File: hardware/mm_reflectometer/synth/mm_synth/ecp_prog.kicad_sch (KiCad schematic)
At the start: 92 parts

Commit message: adding digital connections to synth schematic
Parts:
- removed C? (x3): 100 nF, Capacitor_SMD:C_0402_1005Metric, symbol Device:C
- added C? (x3): 100 nF, symbol Device:C_Small
- added U?: ECP5U_25_CABGA256, Package_BGA:BGA-256_14.0x14.0mm_Layout16x16_P0.8mm_Ball0.45mm_Pad0.32mm_NSMD, symbol Lattice_ECP5:ECP5U_25_CABGA256
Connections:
- net +3V3: now also C?.1, C?.1, C?.1
- net GND: now also C?.2, C?.2, C?.2, U?.A1 (GND[27]), U?.A16 (GND[27]), U?.D15 (GND[27]), U?.D2 (GND[27]), U?.F8 (GND[27]), U?.F9 (GND[27]), U?.G10 (GND[27]), U?.G8 (GND[27]), U?.H1 (GND[27]), U?.H10 (GND[27]), U?.H16 (GND[27]), U?.H8 (GND[27]), U?.H9 (GND[27]), U?.J10 (GND[27]), U?.J8 (GND[27]), U?.J9 (GND[27]), U?.K10 (GND[27]), U?.K6 (GND[27]), U?.K7 (GND[27]), U?.K8 (GND[27]), U?.K9 (GND[27]), U?.N15 (GND[27]), U?.N2 (GND[27]), U?.T1 (GND[27]), U?.T12 (GND[27]), U?.T16 (GND[27]), U?.T5 (GND[27])
- new net +1V1: U?.G6 (VCC[6]), U?.G7 (VCC[6]), U?.G9 (VCC[6]), U?.L10 (VCC[6]), U?.L8 (VCC[6]), U?.L9 (VCC[6])
- new net +2V5: U?.G11 (VCCAUX[2]), U?.L7 (VCCAUX[2])
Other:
- note added: "TODO: ADD RESET BUTTON.."
- note removed: "TODO: ADD RESET.."
- moved on the sheet: R?, TP?, U?H

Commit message: work on mm synth schematic - control signals and footprint assignments
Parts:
- added C1621, C1622: 100 nF, Capacitor_SMD:C_0402_1005Metric, symbol Device:C_Small
- added J1605, J1606: Conn_Coaxial, Connector_Coaxial:U.FL_Hirose_U.FL-R-SMT-1_Vertical, symbol Connector:Conn_Coaxial
- added R1638, R1639: 5.1k, Resistor_SMD:R_0402_1005Metric, symbol Device:R_Small
- added SW1601, SW1602: SW_Push, symbol Switch:SW_Push
- added TP1604: TestPoint, TestPoint:TestPoint_Pad_D1.5mm, symbol Connector:TestPoint
- C1623, C1624, C1625: renamed from C?; footprint (none) -> Capacitor_SMD:C_0402_1005Metric
- U1605: renamed from U?; Notes (none) -> Flash schematic and symbol adapted from Greg Davill's ECPBr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
- gave numbers to parts that had none: 82
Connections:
- net +3V3: now also R1638.1, R1639.1
- net GND: now also C1621.2, C1622.2, J1605.2 (Ext), J1606.2 (Ext), SW1601.1, SW1602.1
- net at U1601.L13 (PR29C/+/GR_PCLK3_1/RDQ32): now also TP1604.1
- net at U1601.B7 (PT27B/-/PCLKC0_1): now also C1622.1, R1639.2, SW1602.2
- net at U1601.C5 (PT15A/+): now also C1621.1, R1638.2, SW1601.2
- net at U1601.D7 (PT24B/-/GR_PCLK0_0): now also J1606.1 (In)
- net at U1601.E7 (PT24A/+/GR_PCLK0_1): now also J1605.1 (In)
- net FLASH_~HLD~|~RST~|IO3 renamed FLASH_~{HLD}|~{RST}|IO3
- net FLASH_~WP~|IO2 renamed FLASH_~{WP}|IO2
- net ~FPGA_RESET renamed ~{FPGA_RESET}
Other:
- note removed: "Flash and sequencer schematic and symbol adapted from Greg Davill's ECPBreaker CC-BY-SA V4.0"
- note removed: "TODO: ADD RESET BUTTON.."
- moved on the sheet: C1625, U1601B

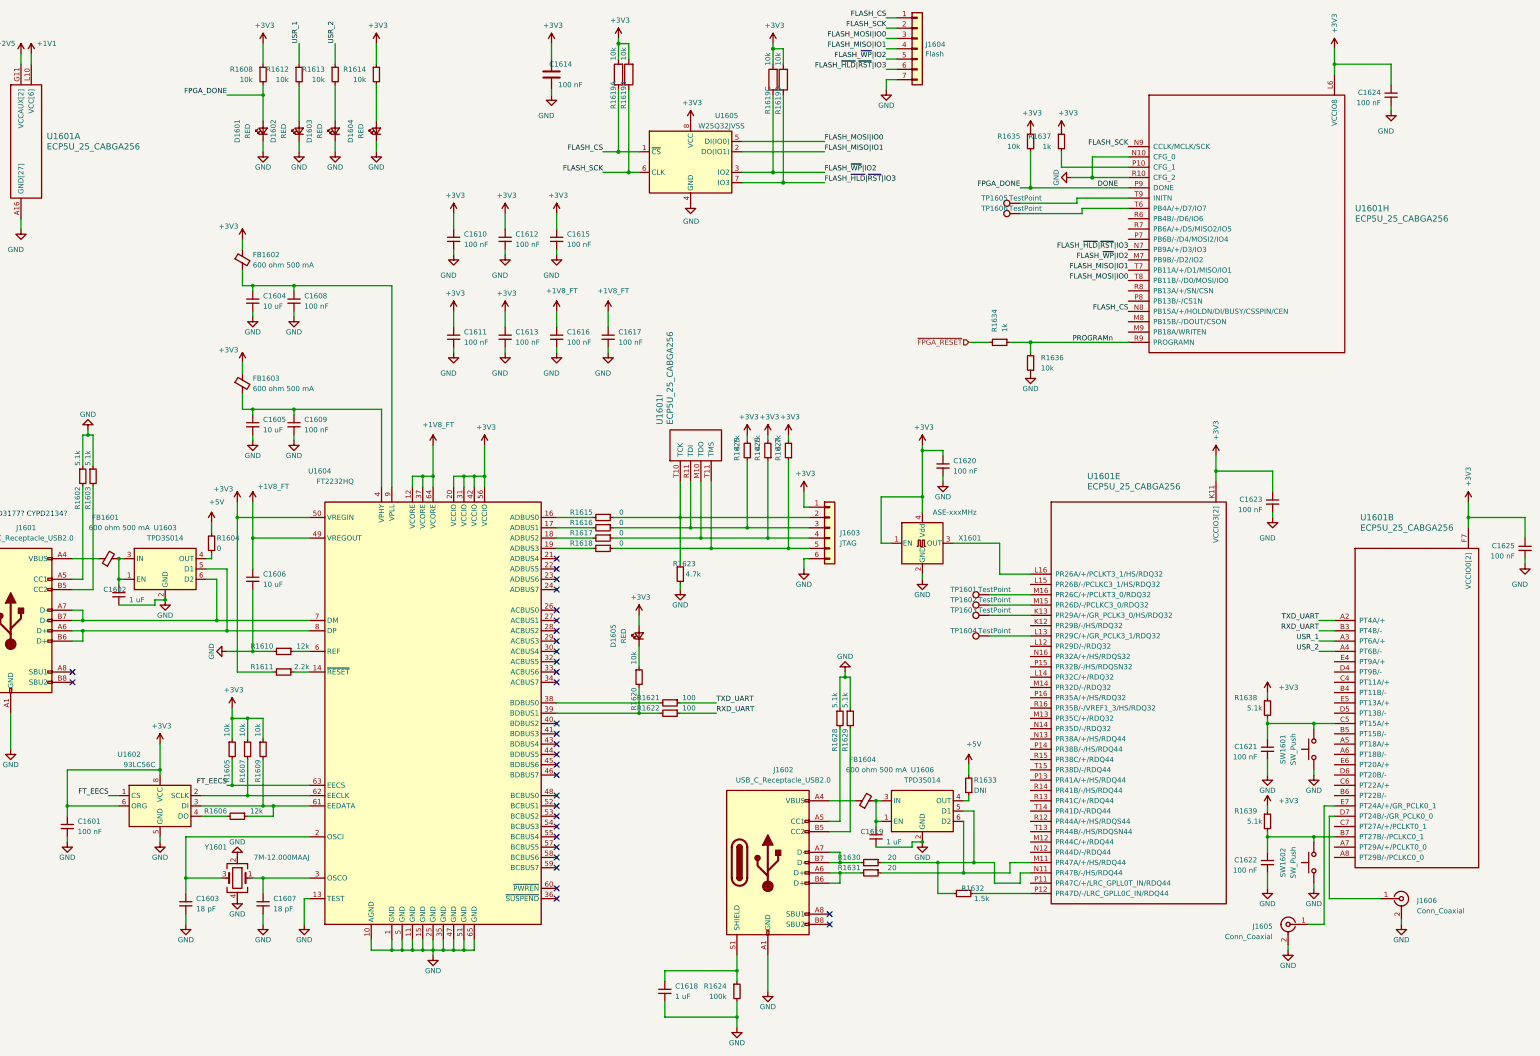
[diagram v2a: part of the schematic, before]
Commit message: added aux high speed io connector, fixed hierarchical buses
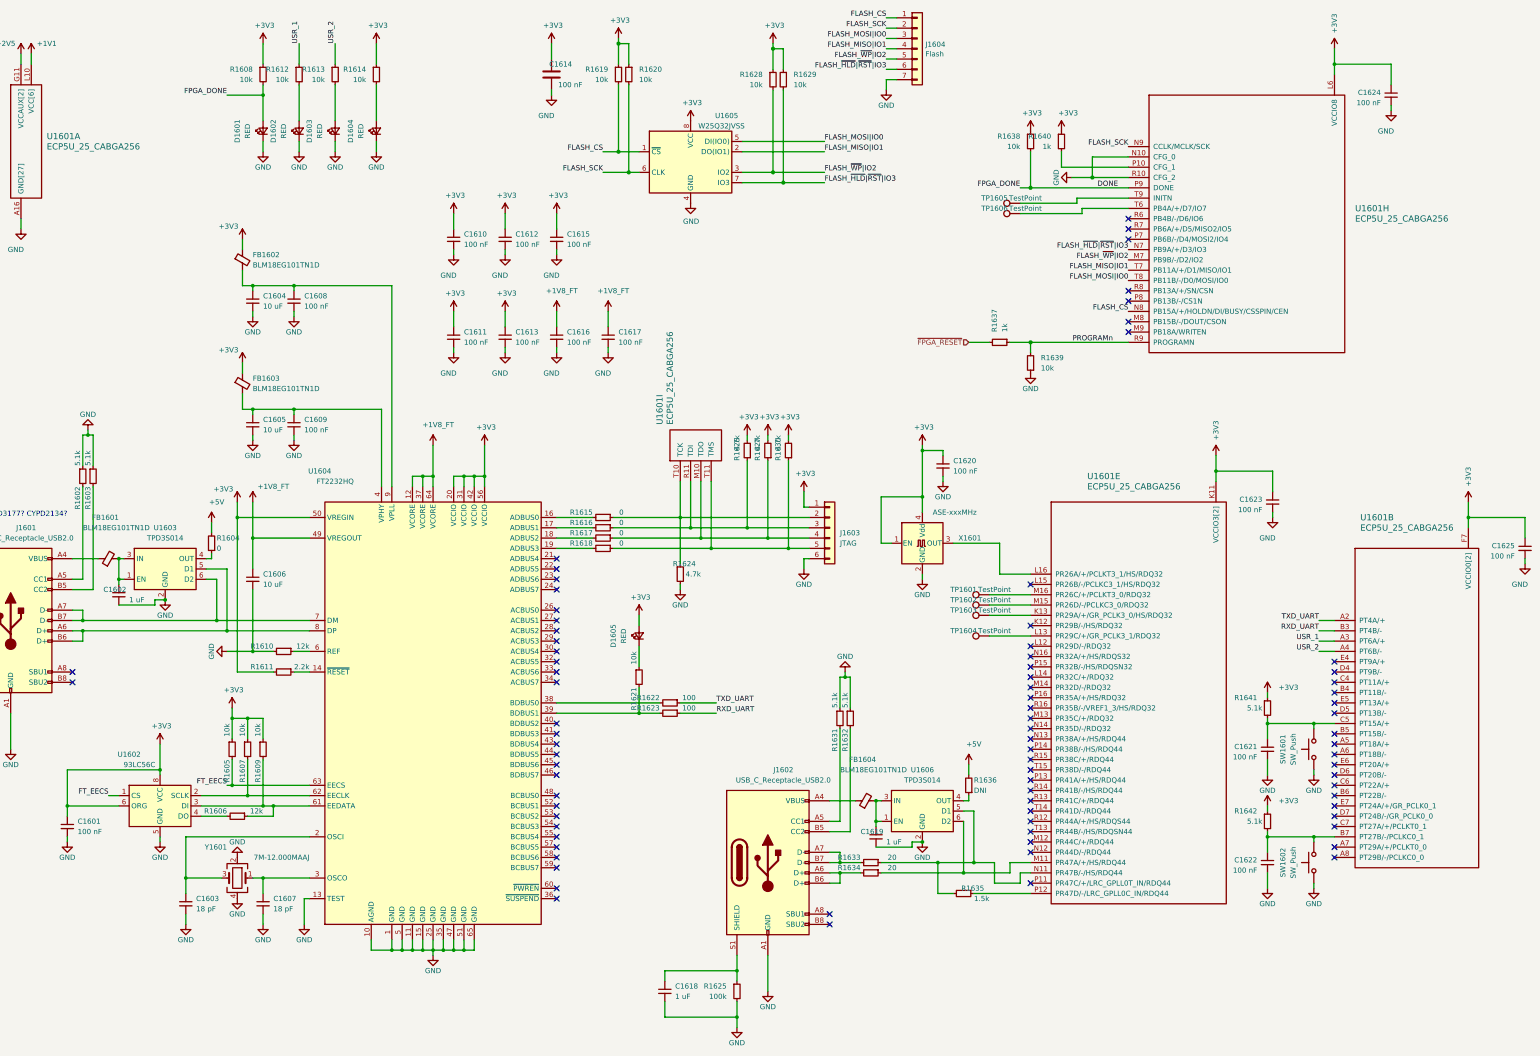
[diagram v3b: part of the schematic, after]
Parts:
- removed J1605, J1606: Conn_Coaxial, Connector_Coaxial:U.FL_Hirose_U.FL-R-SMT-1_Vertical, symbol Connector:Conn_Coaxial
- removed R1619: 10k, Resistor_SMD:R_Array_Convex_4x0402, symbol Device:R_Pack04_Split
- added R1619, R1620, R1628, R1629: 10k, Resistor_SMD:R_0402_1005Metric, symbol Device:R_Small
- FB1601, FB1602, FB1603, FB1604: value 600 ohm 500 mA -> BLM18EG101TN1D
- SW1601, SW1602: footprint (none) -> Button_Switch_SMD:SW_SPST_CK_KXT3
- renumbered R1620 to R1621, R1621 to R1622, R1622 to R1623, R1623 to R1624, R1624 to R1625, R1625 to R1626, R1626 to R1627, R1627 to R1630, R1628 to R1631, R1629 to R1632, R1630 to R1633, R1631 to R1634, R1632 to R1635, R1633 to R1636, R1634 to R1637, R1635 to R1638, R1636 to R1639, R1637 to R1640, R1638 to R1641, R1639 to R1642
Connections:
- net +3V3: now also R1619.1, R1620.1, R1628.1, R1629.1
- net FLASH_CS: now also R1619.2
- net FLASH_SCK: now also R1620.2
- net FLASH_~{HLD}|~{RST}|IO3: now also R1629.2
- net FLASH_~{WP}|IO2: now also R1628.2
- no-connect marks 32 -> 81

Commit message: schematic cleanup, erc
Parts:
- U1601: symbol Lattice_ECP5:ECP5U_25_CABGA256 -> jtk_rf:ECP5U_25_CABGA256
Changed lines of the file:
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@@
     (pin "7")
   )
-  (symbol (lib_id "Lattice_ECP5:ECP5U_25_CABGA256") (at 196.85 135.89 90) (unit 9)
+  (symbol (lib_id "jtk_rf:ECP5U_25_CABGA256") (at 196.85 135.89 90) (unit 9)
     (in_bom yes) (on_board yes)
     (property "Reference" "U1601" (id 0) (at 191.77 121.92 0)
@@
       (effects (font (size 1.524 1.524)) (justify left))
     )
-    (property "Footprint" "Package_BGA:BGA-256_14.0x14.0mm_Layout16x16_P0.8mm_Ball0.45mm_Pad0.32mm_NSMD" (id 2) (at 195.58 132.08 0)
-      (effects (font (size 1.524 1.524)) (justify right) hide)
-    )
-    (property "Datasheet" "" (id 3) (at 200.66 132.08 0)
-      (effects (font (size 1.524 1.524)) (justify right) hide)
-    )
-    (property "manf#" "ECP5U_25" (id 4) (at 198.12 132.08 0)
+    (property "Footprint" "Package_BGA:BGA-256_14.0x14.0mm_Layout16x16_P0.8mm_Ball0.45mm_Pad0.32mm_NSMD" (id 2) (at 195.58 139.7 0)
+      (effects (font (size 1.524 1.524)) (justify right) hide)
+    )
+    (property "Datasheet" "" (id 3) (at 200.66 139.7 0)
+      (effects (font (size 1.524 1.524)) (justify right) hide)
+    )
+    (property "manf#" "ECP5U_25" (id 4) (at 198.12 139.7 0)
       (effects (font (size 1.524 1.524)) (justify right) hide)
     )
@@
     (pin "6")
   )
-  (symbol (lib_id "Lattice_ECP5:ECP5U_25_CABGA256") (at 26.67 55.88 0) (unit 1)
+  (symbol (lib_id "jtk_rf:ECP5U_25_CABGA256") (at 26.67 55.88 0) (unit 1)
     (in_bom yes) (on_board yes)
     (property "Reference" "U1601" (id 0) (at 40.64 50.8 0)
@@
       (effects (font (size 1.524 1.524)) (justify left))
     )
-    (property "Footprint" "Package_BGA:BGA-256_14.0x14.0mm_Layout16x16_P0.8mm_Ball0.45mm_Pad0.32mm_NSMD" (id 2) (at 30.48 54.61 0)
-      (effects (font (size 1.524 1.524)) (justify right) hide)
-    )
-    (property "Datasheet" "" (id 3) (at 30.48 59.69 0)
-      (effects (font (size 1.524 1.524)) (justify right) hide)
-    )
-    (property "manf#" "ECP5U_25" (id 4) (at 30.48 57.15 0)
+    (property "Footprint" "Package_BGA:BGA-256_14.0x14.0mm_Layout16x16_P0.8mm_Ball0.45mm_Pad0.32mm_NSMD" (id 2) (at 22.86 54.61 0)
+      (effects (font (size 1.524 1.524)) (justify right) hide)
+    )
+    (property "Datasheet" "" (id 3) (at 22.86 59.69 0)
+      (effects (font (size 1.524 1.524)) (justify right) hide)
+    )
+    (property "manf#" "ECP5U_25" (id 4) (at 22.86 57.15 0)
       (effects (font (size 1.524 1.524)) (justify right) hide)
     )
@@
     (pin "S1")
   )
-  (symbol (lib_id "Lattice_ECP5:ECP5U_25_CABGA256") (at 358.14 170.18 0) (unit 2)
+  (symbol (lib_id "jtk_rf:ECP5U_25_CABGA256") (at 358.14 170.18 0) (unit 2)
     (in_bom yes) (on_board yes)
     (property "Reference" "U1601" (id 0) (at 364.49 144.78 0)
@@
       (effects (font (size 1.524 1.524)) (justify left))
     )
-    (property "Footprint" "Package_BGA:BGA-256_14.0x14.0mm_Layout16x16_P0.8mm_Ball0.45mm_Pad0.32mm_NSMD" (id 2) (at 361.95 168.91 0)
-      (effects (font (size 1.524 1.524)) (justify right) hide)
-    )
-    (property "Datasheet" "" (id 3) (at 361.95 173.99 0)
-      (effects (font (size 1.524 1.524)) (justify right) hide)
-    )
-    (property "manf#" "ECP5U_25" (id 4) (at 361.95 171.45 0)
+    (property "Footprint" "Package_BGA:BGA-256_14.0x14.0mm_Layout16x16_P0.8mm_Ball0.45mm_Pad0.32mm_NSMD" (id 2) (at 354.33 168.91 0)
+      (effects (font (size 1.524 1.524)) (justify right) hide)
+    )
+    (property "Datasheet" "" (id 3) (at 354.33 173.99 0)
+      (effects (font (size 1.524 1.524)) (justify right) hide)
+    )
+    (property "manf#" "ECP5U_25" (id 4) (at 354.33 171.45 0)
       (effects (font (size 1.524 1.524)) (justify right) hide)
     )
@@
     (pin "F7")
   )
-  (symbol (lib_id "Lattice_ECP5:ECP5U_25_CABGA256") (at 307.34 53.34 0) (unit 8)
+  (symbol (lib_id "jtk_rf:ECP5U_25_CABGA256") (at 307.34 53.34 0) (unit 8)
     (in_bom yes) (on_board yes)
     (property "Reference" "U1601" (id 0) (at 363.22 68.58 0)
@@
       (effects (font (size 1.524 1.524)) (justify left))
     )
-    (property "Footprint" "Package_BGA:BGA-256_14.0x14.0mm_Layout16x16_P0.8mm_Ball0.45mm_Pad0.32mm_NSMD" (id 2) (at 311.15 52.07 0)
-      (effects (font (size 1.524 1.524)) (justify right) hide)
-    )
-    (property "Datasheet" "" (id 3) (at 311.15 57.15 0)
-      (effects (font (size 1.524 1.524)) (justify right) hide)
-    )
-    (property "manf#" "ECP5U_25" (id 4) (at 311.15 54.61 0)
+    (property "Footprint" "Package_BGA:BGA-256_14.0x14.0mm_Layout16x16_P0.8mm_Ball0.45mm_Pad0.32mm_NSMD" (id 2) (at 303.53 52.07 0)
+      (effects (font (size 1.524 1.524)) (justify right) hide)
+    )
+    (property "Datasheet" "" (id 3) (at 303.53 57.15 0)
+      (effects (font (size 1.524 1.524)) (justify right) hide)
+    )
+    (property "manf#" "ECP5U_25" (id 4) (at 303.53 54.61 0)
       (effects (font (size 1.524 1.524)) (justify right) hide)
     )
@@
     (pin "T9")
   )
-  (symbol (lib_id "Lattice_ECP5:ECP5U_25_CABGA256") (at 283.21 158.75 0) (unit 5)
+  (symbol (lib_id "jtk_rf:ECP5U_25_CABGA256") (at 283.21 158.75 0) (unit 5)
     (in_bom yes) (on_board yes)
     (property "Reference" "U1601" (id 0) (at 297.18 134.62 0)
@@
       (effects (font (size 1.524 1.524)) (justify left))
     )
-    (property "Footprint" "Package_BGA:BGA-256_14.0x14.0mm_Layout16x16_P0.8mm_Ball0.45mm_Pad0.32mm_NSMD" (id 2) (at 287.02 157.48 0)
-      (effects (font (size 1.524 1.524)) (justify right) hide)
-    )
-    (property "Datasheet" "" (id 3) (at 287.02 162.56 0)
-      (effects (font (size 1.524 1.524)) (justify right) hide)
-    )
-    (property "manf#" "ECP5U_25" (id 4) (at 287.02 160.02 0)
-      (effects (font (size 1.524 1.524)) (justify right) hide)
-    )
+    (property "Footprint" "Package_BGA:BGA-256_14.0x14.0mm_Layout16x16_P0.8mm_Ball0.45mm_Pad0.32mm_NSMD" (id 2) (at 279.4 157.48 0)
+      (effects (font (size 1.524 1.524)) (justify right) hide)
+    )
+    (property "Datasheet" "" (id 3) (at 279.4 162.56 0)
+      (effects (font (size 1.524 1.524)) (justify right) hide)
+    )
+    (property "manf#" "ECP5U_25" (id 4) (at 279.4 160.02 0)
+      (effects (font (size 1.524 1.524)) (justify right) hide)
+    )

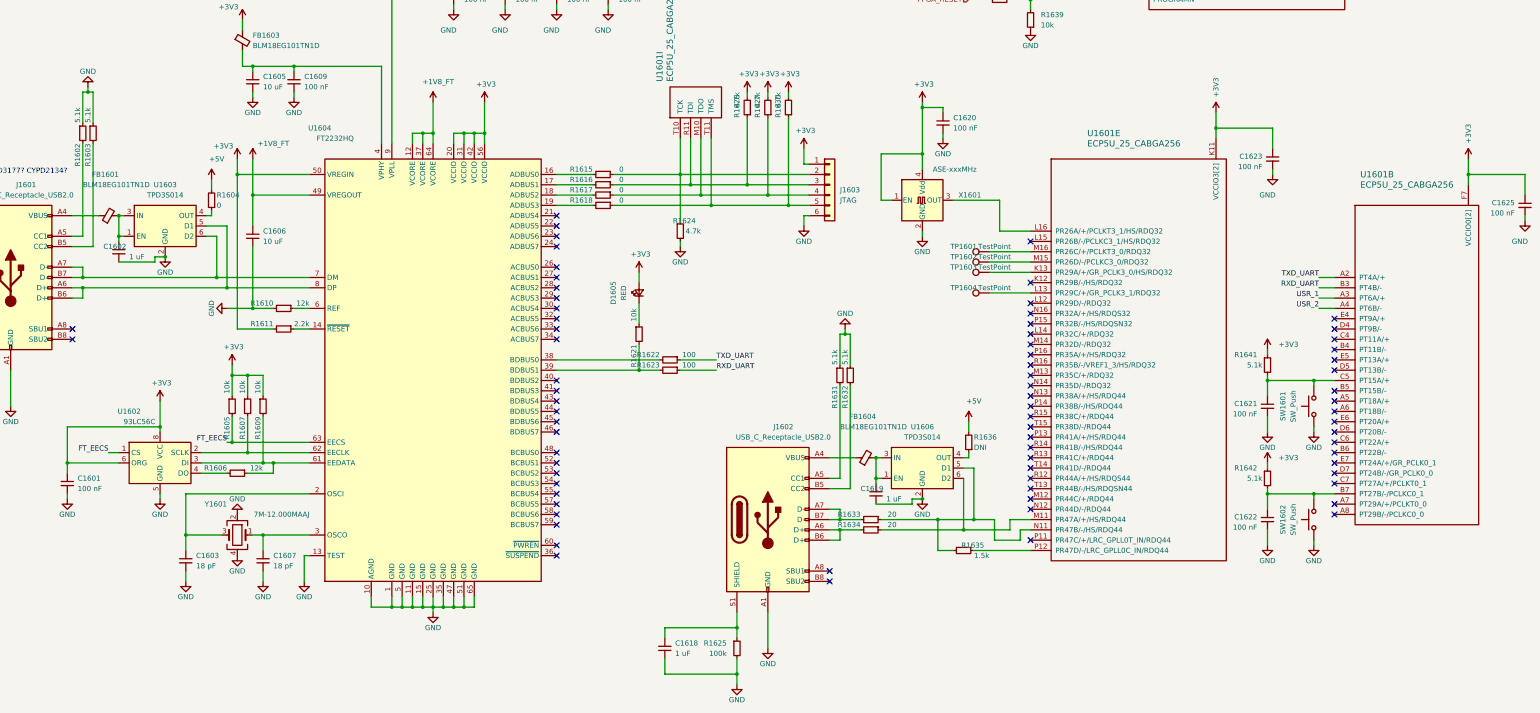
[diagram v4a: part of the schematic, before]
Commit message: added usb PD sink to synth
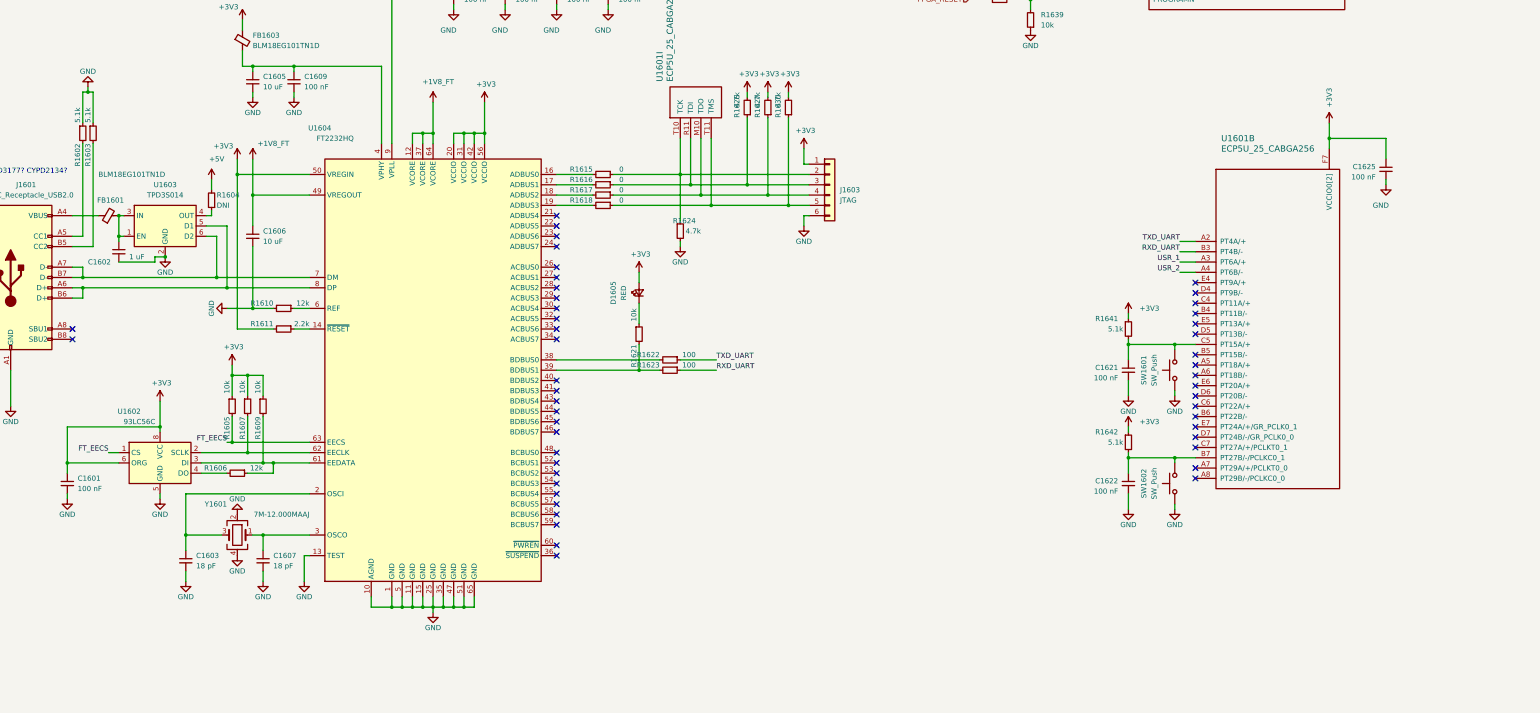
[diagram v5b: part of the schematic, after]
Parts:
- removed C1618, C1619: 1 uF, Capacitor_SMD:C_0402_1005Metric, symbol Device:C_Small
- removed C1620, C1623: 100 nF, Capacitor_SMD:C_0402_1005Metric, symbol Device:C_Small
- removed FB1604: BLM18EG101TN1D, Inductor_SMD:L_0603_1608Metric, symbol Device:FerriteBead_Small
- removed J1602: USB_C_Receptacle_USB2.0, Connector_USB:USB_C_Receptacle_HRO_TYPE-C-31-M-12, symbol Connector:USB_C_Receptacle_USB2.0
- removed R1625: 100k, Resistor_SMD:R_0402_1005Metric, symbol Device:R_Small
- removed R1631, R1632: 5.1k, Resistor_SMD:R_0402_1005Metric, symbol Device:R_Small
- removed R1633, R1634: 20, Resistor_SMD:R_0402_1005Metric, symbol Device:R_Small
- removed R1635: 1.5k, Resistor_SMD:R_0402_1005Metric, symbol Device:R_Small
- removed R1636: DNI, Resistor_SMD:R_0402_1005Metric, symbol Device:R_Small
- removed TP1601, TP1602, TP1603, TP1604: TestPoint, TestPoint:TestPoint_Pad_D1.5mm, symbol Connector:TestPoint
- removed unit 5 of U1601
- removed U1606: TPD3S014, Package_TO_SOT_SMD:SOT-23-6, symbol Power_Protection:TPD3S014
- removed X1601: ASE-xxxMHz, Oscillator:Oscillator_SMD_Abracon_ASE-4Pin_3.2x2.5mm, symbol Oscillator:ASE-xxxMHz
- R1604: value 0 -> DNI
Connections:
- no-connect marks 81 -> 55
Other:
- moved on the sheet: C1621, C1622, C1625, R1641, R1642, SW1601, SW1602, U1601B
